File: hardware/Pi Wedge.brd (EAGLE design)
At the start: 45.7 x 50.8 mm, 13 parts

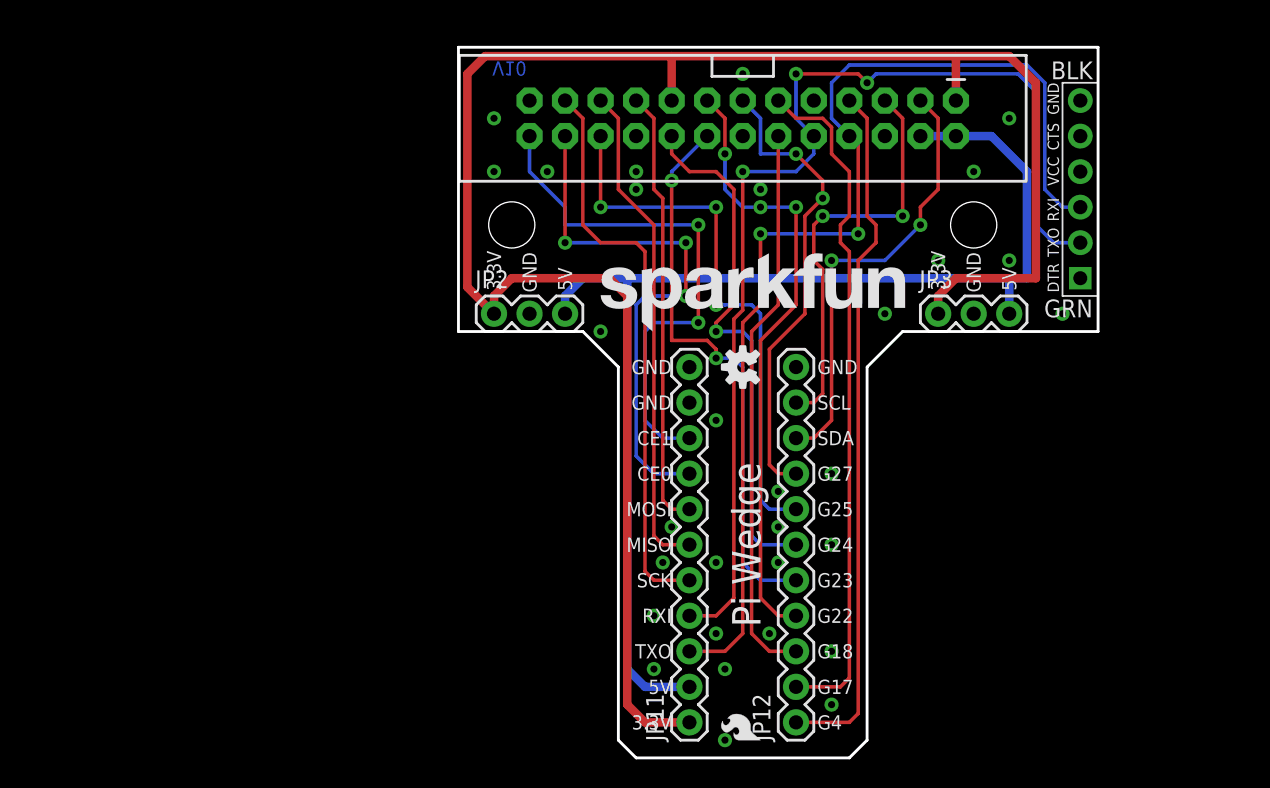
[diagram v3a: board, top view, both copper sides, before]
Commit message: Updates based on group review
Including:
-Kit footprints for the DIP-spaced headers
-Wider overall spacing, so power pads match a breadboard more closely
-PTH decoupling caps on power lines
-Rounded corners.
-Vector text
-Respecting keepout area around standoffs
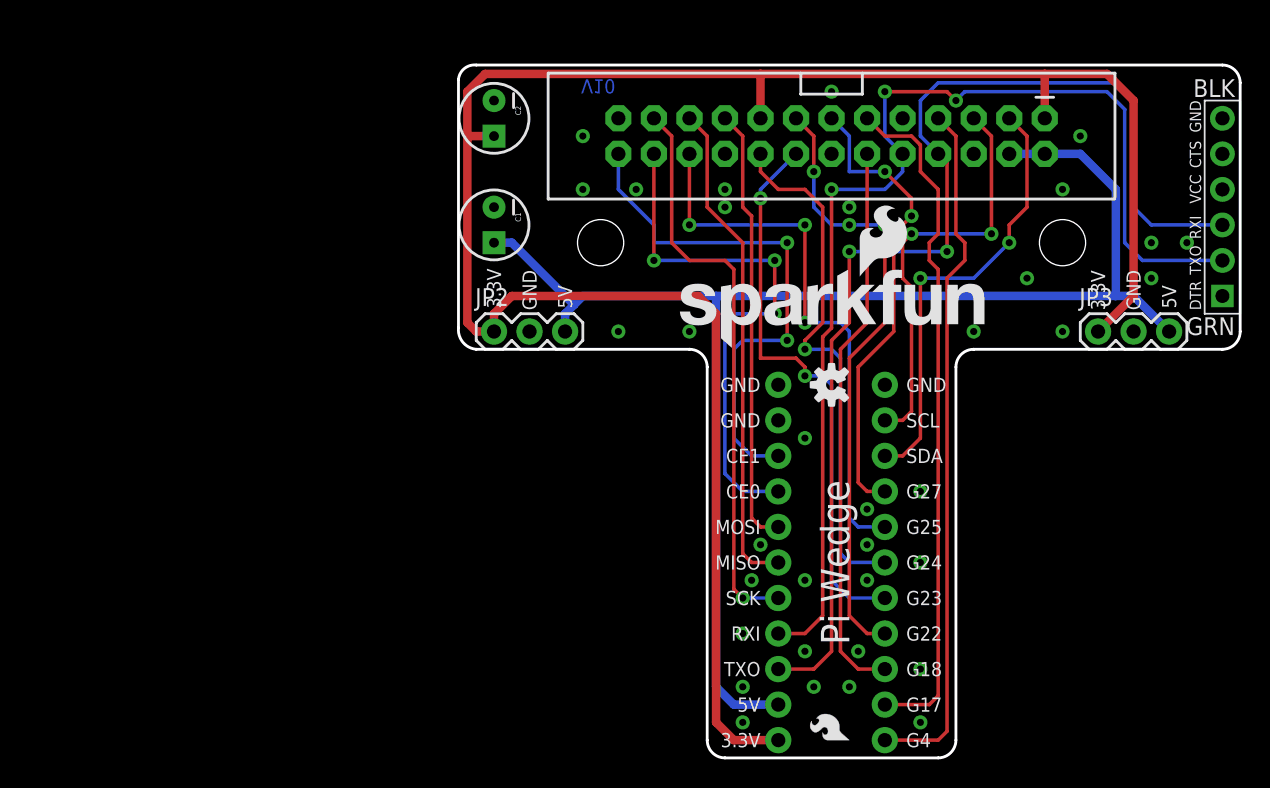
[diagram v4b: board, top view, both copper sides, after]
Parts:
- added C1, C2: 10uf, SparkFun-Capacitors:CPOL-RADIAL-10UF-25V-KIT
- JP11, JP12: value M11PTH -> 1x11 Header; device SparkFun-Connectors:1X11 -> SparkFun-Connectors:1X11_NO_SILK_KIT
- LOGO1: value SFE_LOGO_NAME.2_INCH -> SFE_LOGO_NAME_FLAME.2_INCH; device SparkFun-Aesthetics:SFE_LOGO_NAME_.2 -> SparkFun-Aesthetics:SFE_LOGO_NAME_FLAME_.2
- moved JP3 11.5 mm to (45.7, 30.5)
- moved JP4 10.2 mm to (54.6, 39.4)
- moved FRAME2 9.16 mm to (8.89, -10.2)
- moved JP12 6.48 mm to (30.5, 1.27), flipped to the bottom
- moved STANDOFF2 6.48 mm to (43.2, 36.8)
- moved U$1 6.48 mm to (26.7, 26.7)
- moved JP8 6.48 mm to (26.7, 44.5)
- moved STANDOFF1 6.48 mm to (10.2, 36.8)
- moved JP11 6.48 mm to (22.9, 1.27), flipped to the bottom
- moved JP1 6.35 mm to (27.9, 1.27)
- moved JP5 6.35 mm to (27.3, 1.27)
- moved LOGO1 5.11 mm to (15.1, 29.2)
- moved JP2 1.27 mm to (2.54, 30.5)
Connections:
- net 3.3V: now also C2.1
- net 5V: now also C1.1
- net GND: now also C1.2, C2.2
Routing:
- net 5V: track 86.6 -> 102.8 mm
- net 3.3V: track 135.0 -> 145.8 mm
- net TXO: track 79.0 -> 82.8 mm
- net RXI: track 77.7 -> 81.5 mm
- net SCLK: vias 0 -> 1
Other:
- board size 45.7 x 50.8 mm -> 55.9 x 49.5 mm
- board text added: "Breadboard row spacing:"

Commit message: Touchup to Cap names
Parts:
- renumbered C1 to C5V, C2 to C3V
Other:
- board text added: "C3V"
- board text added: "C5V"
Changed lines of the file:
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@@
 <setting verticaltext="up"/>
 </settings>
-<grid distance="0.1" unitdist="inch" unit="inch" style="lines" multiple="1" display="yes" altdistance="0.025" altunitdist="inch" altunit="inch"/>
+<grid distance="0.05" unitdist="inch" unit="inch" style="lines" multiple="1" display="yes" altdistance="0.005" altunitdist="inch" altunit="inch"/>
 <layers>
 <layer number="1" name="Top" color="4" fill="1" visible="yes" active="yes"/>
@@
 <layer number="27" name="tValues" color="7" fill="1" visible="no" active="yes"/>
 <layer number="28" name="bValues" color="7" fill="1" visible="no" active="yes"/>
-<layer number="29" name="tStop" color="7" fill="3" visible="yes" active="yes"/>
-<layer number="30" name="bStop" color="7" fill="6" visible="yes" active="yes"/>
+<layer number="29" name="tStop" color="7" fill="3" visible="no" active="yes"/>
+<layer number="30" name="bStop" color="7" fill="6" visible="no" active="yes"/>
 <layer number="31" name="tCream" color="7" fill="4" visible="no" active="yes"/>
 <layer number="32" name="bCream" color="7" fill="5" visible="no" active="yes"/>
@@
 <layer number="37" name="tTest" color="7" fill="1" visible="no" active="yes"/>
 <layer number="38" name="bTest" color="7" fill="1" visible="no" active="yes"/>
-<layer number="39" name="tKeepout" color="4" fill="11" visible="yes" active="yes"/>
+<layer number="39" name="tKeepout" color="4" fill="11" visible="no" active="yes"/>
 <layer number="40" name="bKeepout" color="1" fill="11" visible="no" active="yes"/>
 <layer number="41" name="tRestrict" color="4" fill="10" visible="no" active="yes"/>
@@
 <layer number="43" name="vRestrict" color="2" fill="10" visible="no" active="yes"/>
 <layer number="44" name="Drills" color="7" fill="1" visible="no" active="yes"/>
-<layer number="45" name="Holes" color="7" fill="1" visible="no" active="yes"/>
+<layer number="45" name="Holes" color="7" fill="1" visible="yes" active="yes"/>
 <layer number="46" name="Milling" color="3" fill="1" visible="no" active="yes"/>
 <layer number="47" name="Measures" color="7" fill="1" visible="no" active="yes"/>
 <layer number="48" name="Document" color="7" fill="1" visible="no" active="yes"/>
-<layer number="49" name="Reference" color="7" fill="1" visible="no" active="yes"/>
+<layer number="49" name="Reference" color="7" fill="1" visible="yes" active="yes"/>
 <layer number="50" name="dxf" color="7" fill="1" visible="no" active="yes"/>
 <layer number="51" name="tDocu" color="6" fill="1" visible="yes" active="yes"/>
@@
 <text x="50.292" y="32.131" size="1.016" layer="22" font="vector" ratio="19" rot="SMR90">5V</text>
 <text x="26.67" y="53.975" size="1.27" layer="51" font="vector" ratio="15" align="bottom-center">Breadboard row spacing:</text>
+<text x="1.524" y="41.91" size="1.016" layer="21" font="vector" ratio="19" rot="SR0">C3V</text>
+<text x="6.35" y="36.83" size="1.016" layer="21" font="vector" ratio="19" rot="SR90">C5V</text>
 </plain>
 <attributes>
@@
 <element name="STANDOFF2" library="SparkFun-Electromechanical" package="STAND-OFF" value="STAND-OFF" x="43.18" y="36.83"/>
 <element name="JP5" library="SparkFun" package="SFE-LOGO-FLAME" value="LOGO-SFESK" x="27.305" y="1.27" rot="MR0"/>
-<element name="C1" library="SparkFun-Capacitors" package="CPOL-RADIAL-10UF-25V-KIT" value="10uf" x="2.54" y="38.1" rot="R270">
+<element name="C5V" library="SparkFun-Capacitors" package="CPOL-RADIAL-10UF-25V-KIT" value="10uf" x="2.54" y="38.1" rot="R270">
 <attribute name="PROD_ID" value="CAP-08440" x="2.54" y="38.1" size="1.778" layer="27" rot="R270" display="off"/>
 </element>
-<element name="C2" library="SparkFun-Capacitors" package="CPOL-RADIAL-10UF-25V-KIT" value="10uf" x="2.54" y="45.72" rot="R270">
+<element name="C3V" library="SparkFun-Capacitors" package="CPOL-RADIAL-10UF-25V-KIT" value="10uf" x="2.54" y="45.72" rot="R270">
 <attribute name="PROD_ID" value="CAP-08440" x="2.54" y="45.72" size="1.778" layer="27" rot="R270" display="off"/>
 </element>
@@
 <via x="43.18" y="30.48" extent="1-16" drill="0.508"/>
 <via x="8.89" y="40.64" extent="1-16" drill="0.508"/>
-<contactref element="C2" pad="2"/>
-<contactref element="C1" pad="2"/>
+<contactref element="C3V" pad="2"/>
+<contactref element="C5V" pad="2"/>
 <via x="49.53" y="36.83" extent="1-16" drill="0.508"/>
 <via x="52.07" y="36.83" extent="1-16" drill="0.508"/>
@@
 <wire x1="19.685" y1="3.81" x2="18.415" y2="5.08" width="0.6096" layer="16"/>
 <wire x1="18.415" y1="5.08" x2="18.415" y2="33.02" width="0.6096" layer="16"/>
-<contactref element="C1" pad="1"/>
+<contactref element="C5V" pad="1"/>
 <wire x1="2.54" y1="36.83" x2="3.81" y2="36.83" width="0.6096" layer="16"/>
 <wire x1="3.81" y1="36.83" x2="8.255" y2="32.385" width="0.6096" layer="16"/>
@@
 <wire x1="3.81" y1="33.02" x2="2.54" y2="31.75" width="0.6096" layer="1"/>
 <wire x1="2.54" y1="31.75" x2="2.54" y2="30.48" width="0.6096" layer="1"/>
-<contactref element="C2" pad="1"/>
+<contactref element="C3V" pad="1"/>
 <wire x1="2.54" y1="44.45" x2="0.635" y2="44.45" width="0.6096" layer="1"/>
 </signal>

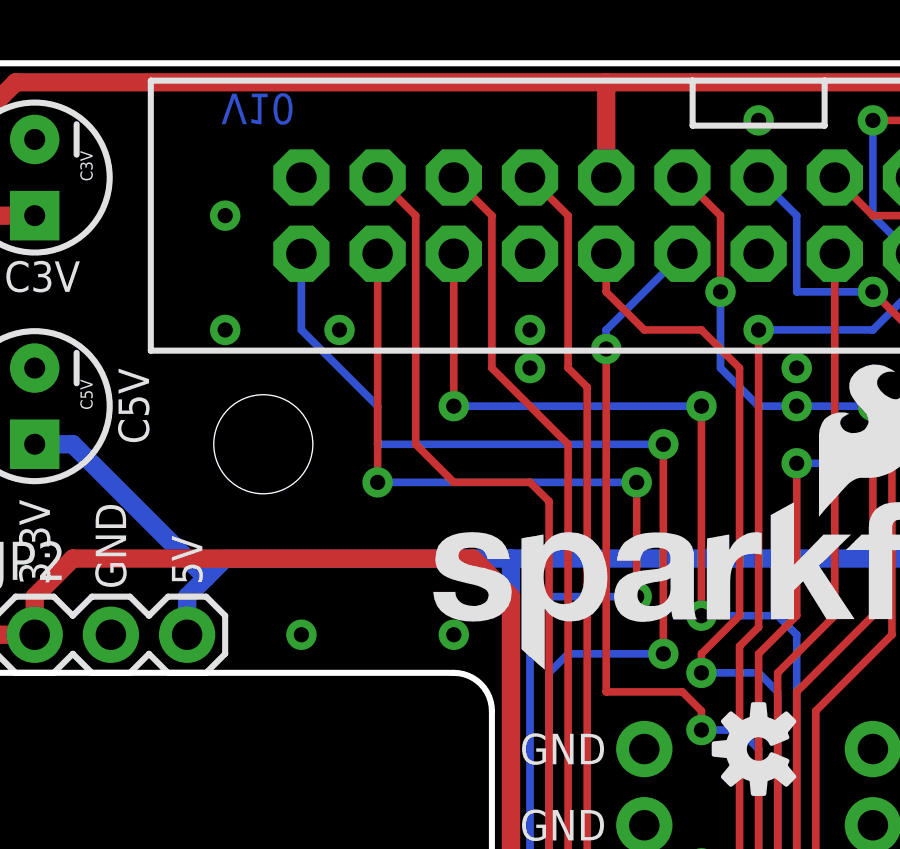
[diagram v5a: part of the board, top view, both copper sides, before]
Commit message: v1.1: Fixing airwire in ground pour.
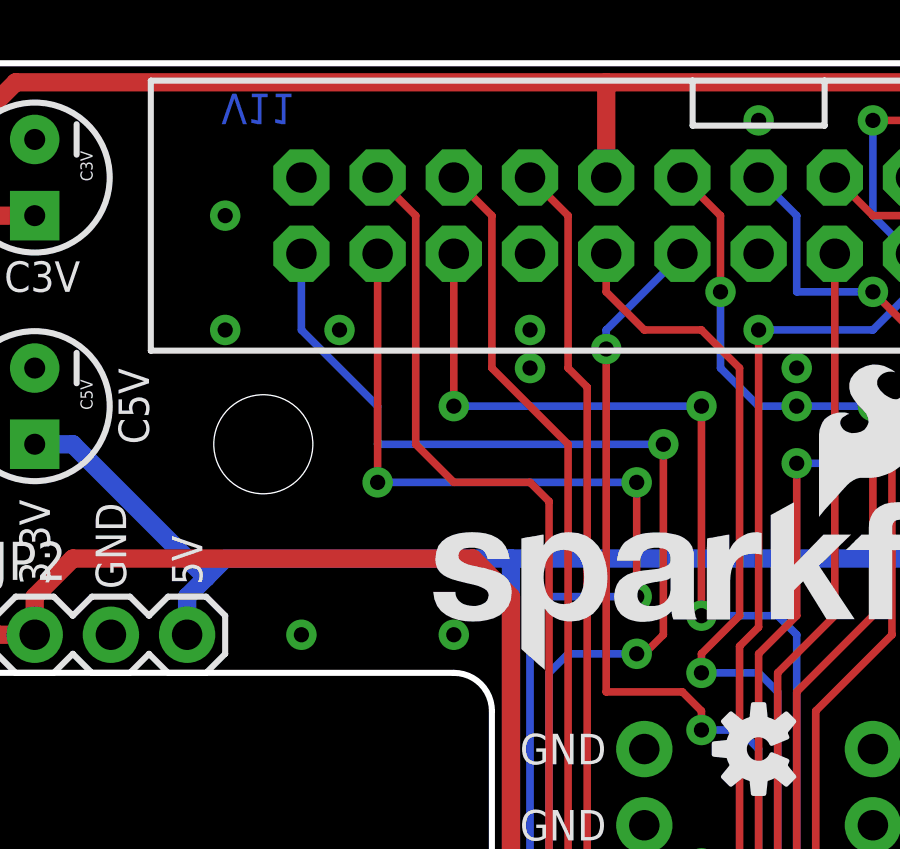
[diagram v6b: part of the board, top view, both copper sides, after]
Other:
- board text added: "V11"
- board text removed: "V10"
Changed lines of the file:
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@@
 <wire x1="0" y1="48.514" x2="0" y2="30.734" width="0.2032" layer="20"/>
 <wire x1="0" y1="30.734" x2="1.27" y2="29.21" width="0.2032" layer="20" curve="90"/>
-<text x="8.763" y="48.514" size="1.016" layer="16" font="vector" ratio="20" rot="SMR180">V10</text>
+<text x="8.763" y="48.514" size="1.016" layer="16" font="vector" ratio="20" rot="SMR180">V11</text>
 <text x="32.004" y="26.67" size="1.016" layer="21" font="vector" ratio="19" rot="SR0" align="center-left">GND</text>
 <text x="21.59" y="26.67" size="1.016" layer="21" font="vector" ratio="19" rot="SR0" align="center-right">GND</text>
@@
 </class>
 </classes>
-<designrules name="SparkFun-2-layer">
+<designrules name="SparkFun-2-layer *">
 <description language="en">&lt;b&gt;EAGLE Design Rules&lt;/b&gt;
 &lt;p&gt;
@@
 <param name="dpGapFactor" value="2.5"/>
 <param name="checkGrid" value="0"/>
-<param name="checkAngle" value="0"/>
+<param name="checkAngle" value="1"/>
 <param name="checkFont" value="1"/>
 <param name="checkRestrict" value="1"/>
@@
 <via x="11.43" y="30.48" extent="1-16" drill="0.508"/>
 <via x="20.32" y="2.54" extent="1-16" drill="0.508"/>
-<wire x1="24.765" y1="12.7" x2="20.955" y2="12.7" width="0" layer="19" extent="1-1"/>
 </signal>
 <signal name="5V">
@@
 <wire x1="19.685" y1="22.86" x2="19.685" y2="29.21" width="0.254" layer="16"/>
 <wire x1="19.685" y1="29.21" x2="20.32" y2="29.845" width="0.254" layer="16"/>
-<wire x1="20.32" y1="29.845" x2="23.495" y2="29.845" width="0.254" layer="16"/>
-<via x="23.495" y="29.845" extent="1-16" drill="0.508"/>
-<wire x1="23.495" y1="29.845" x2="23.495" y2="36.83" width="0.254" layer="1"/>
+<wire x1="20.32" y1="29.845" x2="22.606" y2="29.845" width="0.254" layer="16"/>
+<via x="22.606" y="29.845" extent="1-16" drill="0.508"/>
+<wire x1="22.606" y1="29.845" x2="22.86" y2="29.845" width="0.254" layer="1"/>
+<wire x1="22.86" y1="29.845" x2="23.495" y2="30.48" width="0.254" layer="1"/>
+<wire x1="23.495" y1="30.48" x2="23.495" y2="36.83" width="0.254" layer="1"/>
 <via x="23.495" y="36.83" extent="1-16" drill="0.508"/>
 <wire x1="23.495" y1="36.83" x2="13.97" y2="36.83" width="0.254" layer="16"/>
